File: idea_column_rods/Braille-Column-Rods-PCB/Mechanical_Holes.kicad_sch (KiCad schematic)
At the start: 14 parts

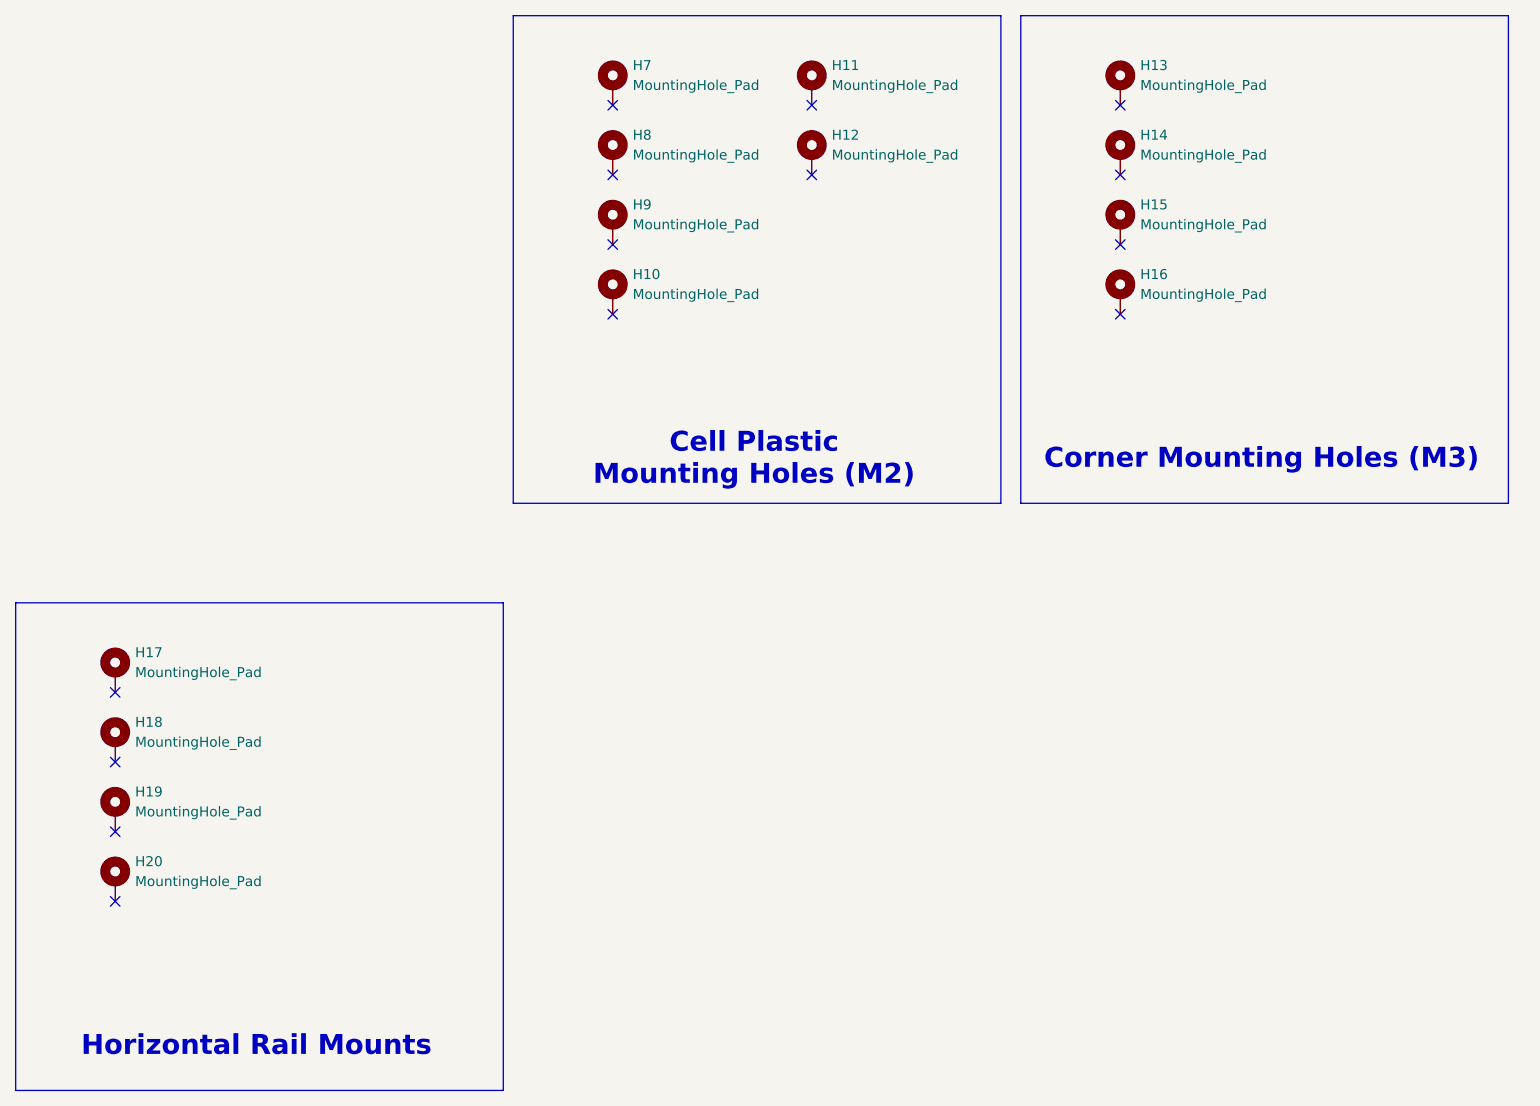
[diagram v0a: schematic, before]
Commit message: Create PCB and CAD for Type 4 Rev 1 rod cams (#13)
* WIP: Rods PCB placement

* WIP: Place the housing and motor X

* WIP: Position everything

* WIP: Update tight placement of DC motor

* WIP: Layout and route the stepper driver

* WIP: Motor layout is good

* WIP: Manual routing and silkscreens

* Comments

* Big routing

* Clean up DRC (mostly footprints)

* Fix spacing issue on top

* Fix spacing issues on bottom

* Create render of 6mm motor, add to PCB

* WIP: Get cams good

* WIP: Reorder the cam bushing and hall sensor

* Finish and tag release

* Complete type 4 rev 1

* Create dc_motor_clamp cad
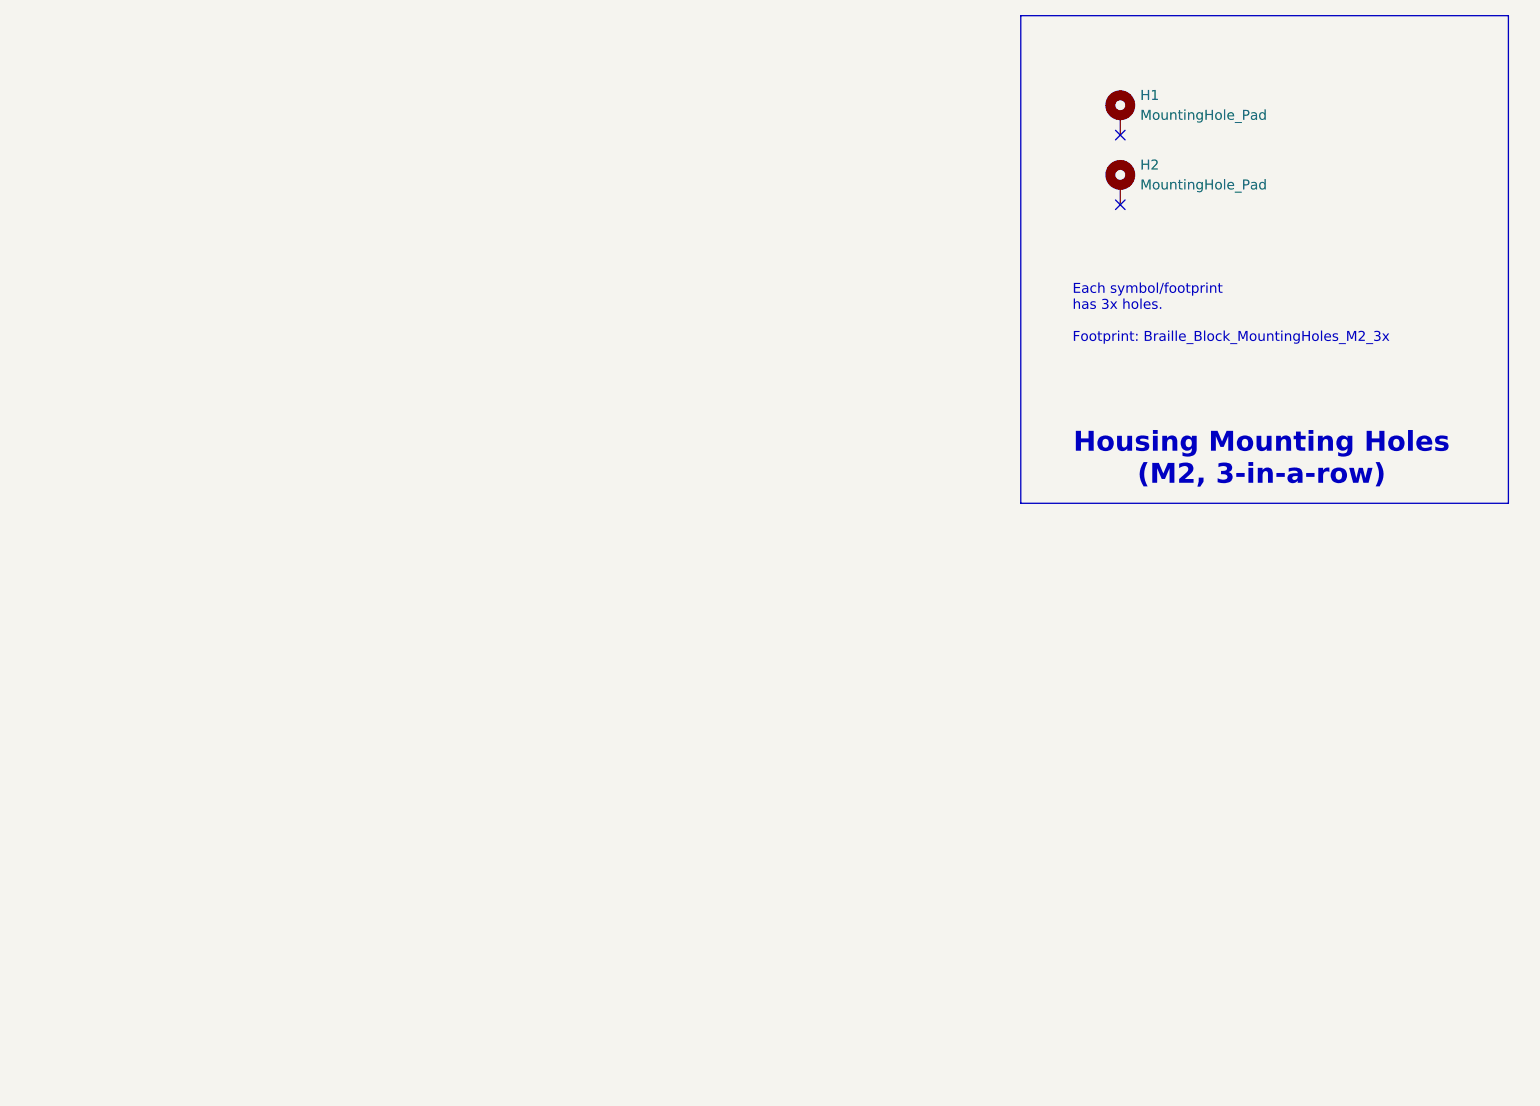
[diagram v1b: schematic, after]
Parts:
- removed H10, H11, H12, H7, H8, H9: MountingHole_Pad, 00-lib-footprints:MountingHole_2.2mm_M2_Pad_NoSilk, symbol Mechanical:MountingHole_Pad
- removed H13, H14, H15, H16: MountingHole_Pad, 00-lib-footprints:MountingHole_3.2mm_M3_Pad_NoSilk, symbol Mechanical:MountingHole_Pad
- removed H17, H18, H19, H20: MountingHole_Pad, 00-lib-footprints:HorizMounting_4x_M2_and_M3_Middle, symbol Mechanical:MountingHole_Pad
- added H1, H2: MountingHole_Pad, 00-lib-footprints:Braille_Block_MountingHoles_M2_3x, symbol Mechanical:MountingHole_Pad
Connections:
- no-connect marks 14 -> 2
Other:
- note added: "Each symbol/footprint has 3x holes. Footprint: Braille_Block_MountingHoles_M2_3x"
- note added: "Housing Mounting Holes (M2, 3-in-a-row)"
- note removed: "Cell Plastic Mounting Holes (M2)"
- note removed: "Corner Mounting Holes (M3)"
- note removed: "Horizontal Rail Mounts"
- title: (none) -> Braille Cam Rod Prototype (Type 4)
